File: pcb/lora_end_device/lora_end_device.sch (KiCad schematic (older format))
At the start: 27 parts, among them J1 USB_B_Micro, J2 UFL, J3 SMA, J4 UART, J5 Reset, J6 PRG, U1 TC1047A, U2 MCP6021, U3 LD1117, U4 RFM95W-868S2_mcc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

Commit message: fix bugs ERC
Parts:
- removed J1: USB_B_Micro, Connector_USB:USB_Micro-B_Molex-105133-0031, symbol Connector:USB_B_Micro
- added J1: USB_B_Micro, symbol Conector:USB_B_Micro
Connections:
- net GND: now also J1.5 (GND), J1.6 (Shield)
- net at D1.2 (A): now also J1.1 (VBUS)
- no-connect marks 0 -> 7
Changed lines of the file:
@@
-$EndComp
-$Comp
-L Diode:1N4007 D1
-U 1 1 60DF922B
-P 2550 6100
-F 0 "D1" H 2550 5883 50  0000 C CNN
-F 1 "1N4007" H 2550 5974 50  0000 C CNN
-F 2 "Diode_SMD:D_1206_3216Metric" H 2550 5925 50  0001 C CNN
-F 3 "http://www.vishay.com/docs/88503/1n4001.pdf" H 2550 6100 50  0001 C CNN
-	1    2550 6100
-	-1   0    0    1
 $EndComp
 $Comp
@@
 $EndComp
 $Comp
-L Connector:USB_B_Micro J1
-U 1 1 60DFF0A9
-P 1850 6300
-F 0 "J1" H 1907 6767 50  0000 C CNN
-F 1 "USB_B_Micro" H 1907 6676 50  0000 C CNN
-F 2 "Connector_USB:USB_Micro-B_Molex-105133-0031" H 2000 6250 50  0001 C CNN
-F 3 "~" H 2000 6250 50  0001 C CNN
-	1    1850 6300
-	1    0    0    -1
-$EndComp
-$Comp
-L power:GND #PWR03
-U 1 1 60EC034B
-P 1850 7000
-F 0 "#PWR03" H 1850 6750 50  0001 C CNN
-F 1 "GND" H 1855 6827 50  0000 C CNN
-F 2 "" H 1850 7000 50  0001 C CNN
-F 3 "" H 1850 7000 50  0001 C CNN
-	1    1850 7000
-	1    0    0    -1
-$EndComp
-$Comp
 L power:GND #PWR04
 U 1 1 60EC08DB
@@
 F 3 "" H 3350 6500 50  0001 C CNN
 	1    3350 6500
-	1    0    0    -1
-$EndComp
-$Comp
-L power:GND #PWR07
-U 1 1 60EC17F2
-P 4000 6500
-F 0 "#PWR07" H 4000 6250 50  0001 C CNN
-F 1 "GND" H 4005 6327 50  0000 C CNN
-F 2 "" H 4000 6500 50  0001 C CNN
-F 3 "" H 4000 6500 50  0001 C CNN
-	1    4000 6500
 	1    0    0    -1
 $EndComp
@@
 	2000 3450 2000 3250
 Wire Wire Line
-	2150 6100 2400 6100
-Wire Wire Line
-	2700 6100 2900 6100
-Wire Wire Line
 	2900 6100 3350 6100
 Connection ~ 2900 6100
 Wire Wire Line
-	3350 6100 3700 6100
-Connection ~ 3350 6100
-Wire Wire Line
 	4300 6100 4600 6100
-Wire Wire Line
-	1750 6700 1750 6750
-Wire Wire Line
-	1750 6750 1850 6750
-Wire Wire Line
-	1850 6750 1850 6700
-Wire Wire Line
-	1850 6750 1850 7000
-Connection ~ 1850 6750
 Wire Wire Line
 	4600 6100 4600 5700
 Connection ~ 4600 6100
-Wire Wire Line
-	4600 6400 4600 6500
 Wire Wire Line
 	4000 6400 4000 6500
@@
 	5600 1650 5600 2100
 Wire Notes Line
-	5250 5250 5250 7350
-Wire Notes Line
 	1300 5250 5250 5250
 Wire Wire Line
-	9950 3900 9950 4000
-Wire Wire Line
-	10050 3900 9950 3900
-Wire Wire Line
 	9950 4600 9950 4700
 Wire Wire Line
 	10050 4600 9950 4600
 $Comp
-L power:GND #PWR?
+L power:GND #PWR0101
 U 1 1 61107347
 P 9950 4700
-F 0 "#PWR?" H 9950 4450 50  0001 C CNN
+F 0 "#PWR0101" H 9950 4450 50  0001 C CNN
 F 1 "GND" H 9955 4527 50  0000 C CNN
 F 2 "" H 9950 4700 50  0001 C CNN
@@
 $EndComp
 $Comp
-L power:GND #PWR?
+L power:GND #PWR0102
 U 1 1 61106BAC
-P 9950 4000
-F 0 "#PWR?" H 9950 3750 50  0001 C CNN
-F 1 "GND" H 9955 3827 50  0000 C CNN
-F 2 "" H 9950 4000 50  0001 C CNN
-F 3 "" H 9950 4000 50  0001 C CNN
-	1    9950 4000
+P 9950 4100
+F 0 "#PWR0102" H 9950 3850 50  0001 C CNN
+F 1 "GND" H 9955 3927 50  0000 C CNN
+F 2 "" H 9950 4100 50  0001 C CNN
+F 3 "" H 9950 4100 50  0001 C CNN
+	1    9950 4100
 	1    0    0    -1
 $EndComp
@@
 Conectores de antena
 $Comp
-L power:GND #PWR?
+L power:GND #PWR0103
 U 1 1 611C175D
 P 3650 4200
-F 0 "#PWR?" H 3650 3950 50  0001 C CNN
+F 0 "#PWR0103" H 3650 3950 50  0001 C CNN
 F 1 "GND" H 3655 4027 50  0000 C CNN
 F 2 "" H 3650 4200 50  0001 C CNN
@@
 $EndComp
 $Comp
-L power:+3.3V #PWR?
+L power:+3.3V #PWR0104
 U 1 1 611C2640
 P 3650 3050
-F 0 "#PWR?" H 3650 2900 50  0001 C CNN
+F 0 "#PWR0104" H 3650 2900 50  0001 C CNN
 F 1 "+3.3V" H 3665 3223 50  0000 C CNN
 F 2 "" H 3650 3050 50  0001 C CNN
@@
 Wire Wire Line
 	6000 4400 7750 4400
+NoConn ~ 6350 3350
+NoConn ~ 6350 3450
+NoConn ~ 6350 3550
+NoConn ~ 6350 3650
+NoConn ~ 2150 6300
+NoConn ~ 2150 6400
+NoConn ~ 2150 6500
+Wire Wire Line
+	3350 6100 3550 6100
+Connection ~ 3350 6100
+Wire Wire Line
+	1850 6700 1850 6800
+$Comp
+L Conector:USB_B_Micro J1
+U 1 1 6125ECC1
+P 1850 6300
+F 0 "J1" H 1907 6767 50  0000 C CNN
+F 1 "USB_B_Micro" H 1907 6676 50  0000 C CNN
+F 2 "" H 2000 6250 50  0001 C CNN
+F 3 "~" H 2000 6250 50  0001 C CNN
+	1    1850 6300
+	1    0    0    -1
+$EndComp
+Wire Wire Line
+	1750 6700 1750 6800
+Wire Wire Line
+	1750 6800 1850 6800
+Wire Wire Line
+	2700 6100 2900 6100
+Wire Wire Line
+	2150 6100 2400 6100
+$Comp
+L Diode:1N4007 D1
+U 1 1 60DF922B
+P 2550 6100
+F 0 "D1" H 2550 5883 50  0000 C CNN
+F 1 "1N4007" H 2550 5974 50  0000 C CNN
+F 2 "Diode_SMD:D_1206_3216Metric" H 2550 5925 50  0001 C CNN
+F 3 "http://www.vishay.com/docs/88503/1n4001.pdf" H 2550 6100 50  0001 C CNN
+	1    2550 6100
+	-1   0    0    1
+$EndComp
+Connection ~ 1850 6800
+$Comp
+L power:GND #PWR03
+U 1 1 60EC034B
+P 1850 7100
+F 0 "#PWR03" H 1850 6850 50  0001 C CNN
+F 1 "GND" H 1855 6927 50  0000 C CNN
+F 2 "" H 1850 7100 50  0001 C CNN
+F 3 "" H 1850 7100 50  0001 C CNN
+	1    1850 7100
+	1    0    0    -1
+$EndComp
+Wire Wire Line
+	1850 6800 1850 7100
+Wire Wire Line
+	10050 3900 9950 3900
+Wire Wire Line
+	9950 3900 9950 4100
+Wire Wire Line
+	3550 5950 3550 6100
+Connection ~ 3550 6100
+Wire Wire Line
+	3550 6100 3700 6100
+$Comp
+L power:PWR_FLAG #FLG0101
+U 1 1 612BB4E2
+P 3550 5950
+F 0 "#FLG0101" H 3550 6025 50  0001 C CNN
+F 1 "PWR_FLAG" H 3550 6123 50  0000 C CNN
+F 2 "" H 3550 5950 50  0001 C CNN
+F 3 "~" H 3550 5950 50  0001 C CNN
+	1    3550 5950
+	1    0    0    -1
+$EndComp
+Wire Notes Line
+	5250 5250 5250 7350
+Wire Wire Line
+	4600 6400 4600 6500
+$Comp
+L power:GND #PWR07
+U 1 1 60EC17F2
+P 4000 6500
+F 0 "#PWR07" H 4000 6250 50  0001 C CNN
+F 1 "GND" H 4005 6327 50  0000 C CNN
+F 2 "" H 4000 6500 50  0001 C CNN
+F 3 "" H 4000 6500 50  0001 C CNN
+	1    4000 6500
+	1    0    0    -1
+$EndComp
+$Comp
+L power:PWR_FLAG #FLG0102
+U 1 1 60E3DDB4
+P 5000 6850
+F 0 "#FLG0102" H 5000 6925 50  0001 C CNN
+F 1 "PWR_FLAG" H 5000 7023 50  0000 C CNN
+F 2 "" H 5000 6850 50  0001 C CNN
+F 3 "~" H 5000 6850 50  0001 C CNN
+	1    5000 6850
+	1    0    0    -1
+$EndComp
+$Comp
+L power:GND #PWR0105
+U 1 1 60E3E607
+P 5000 7050
+F 0 "#PWR0105" H 5000 6800 50  0001 C CNN
+F 1 "GND" H 5005 6877 50  0000 C CNN
+F 2 "" H 5000 7050 50  0001 C CNN
+F 3 "" H 5000 7050 50  0001 C CNN
+	1    5000 7050
+	1    0    0    -1
+$EndComp
+Wire Wire Line
+	5000 6850 5000 7050
 $EndSCHEMATC

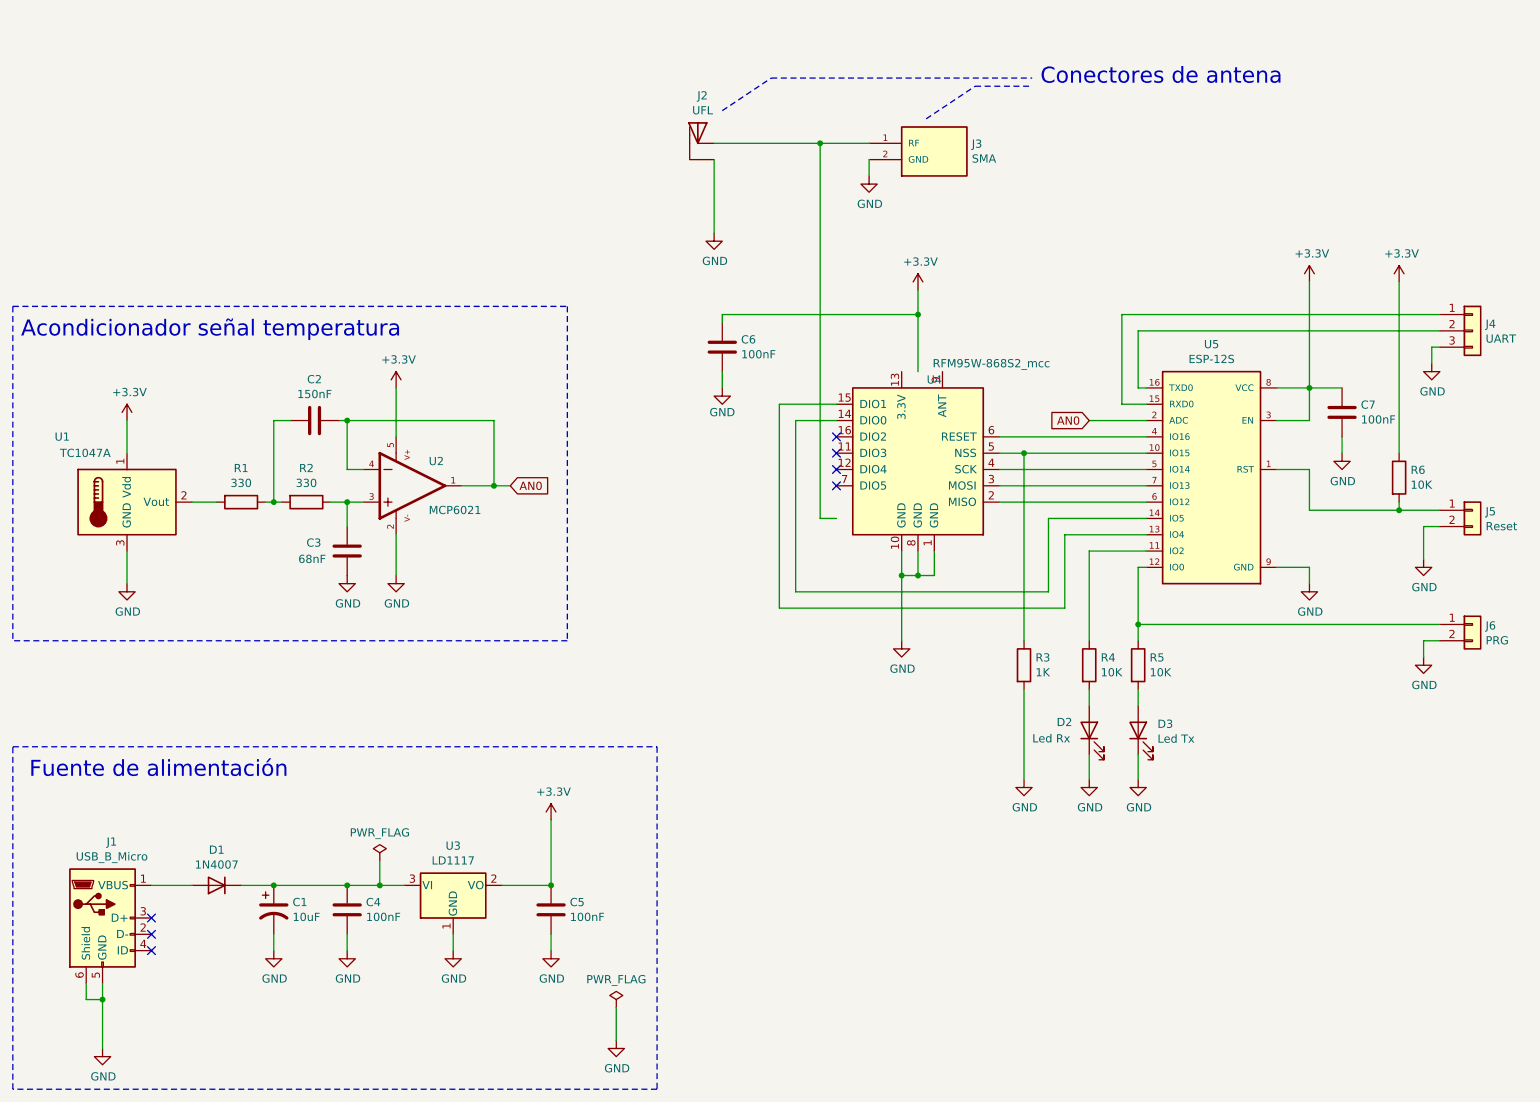
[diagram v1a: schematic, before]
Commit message: add asociaciones footprint, orificios fijacion
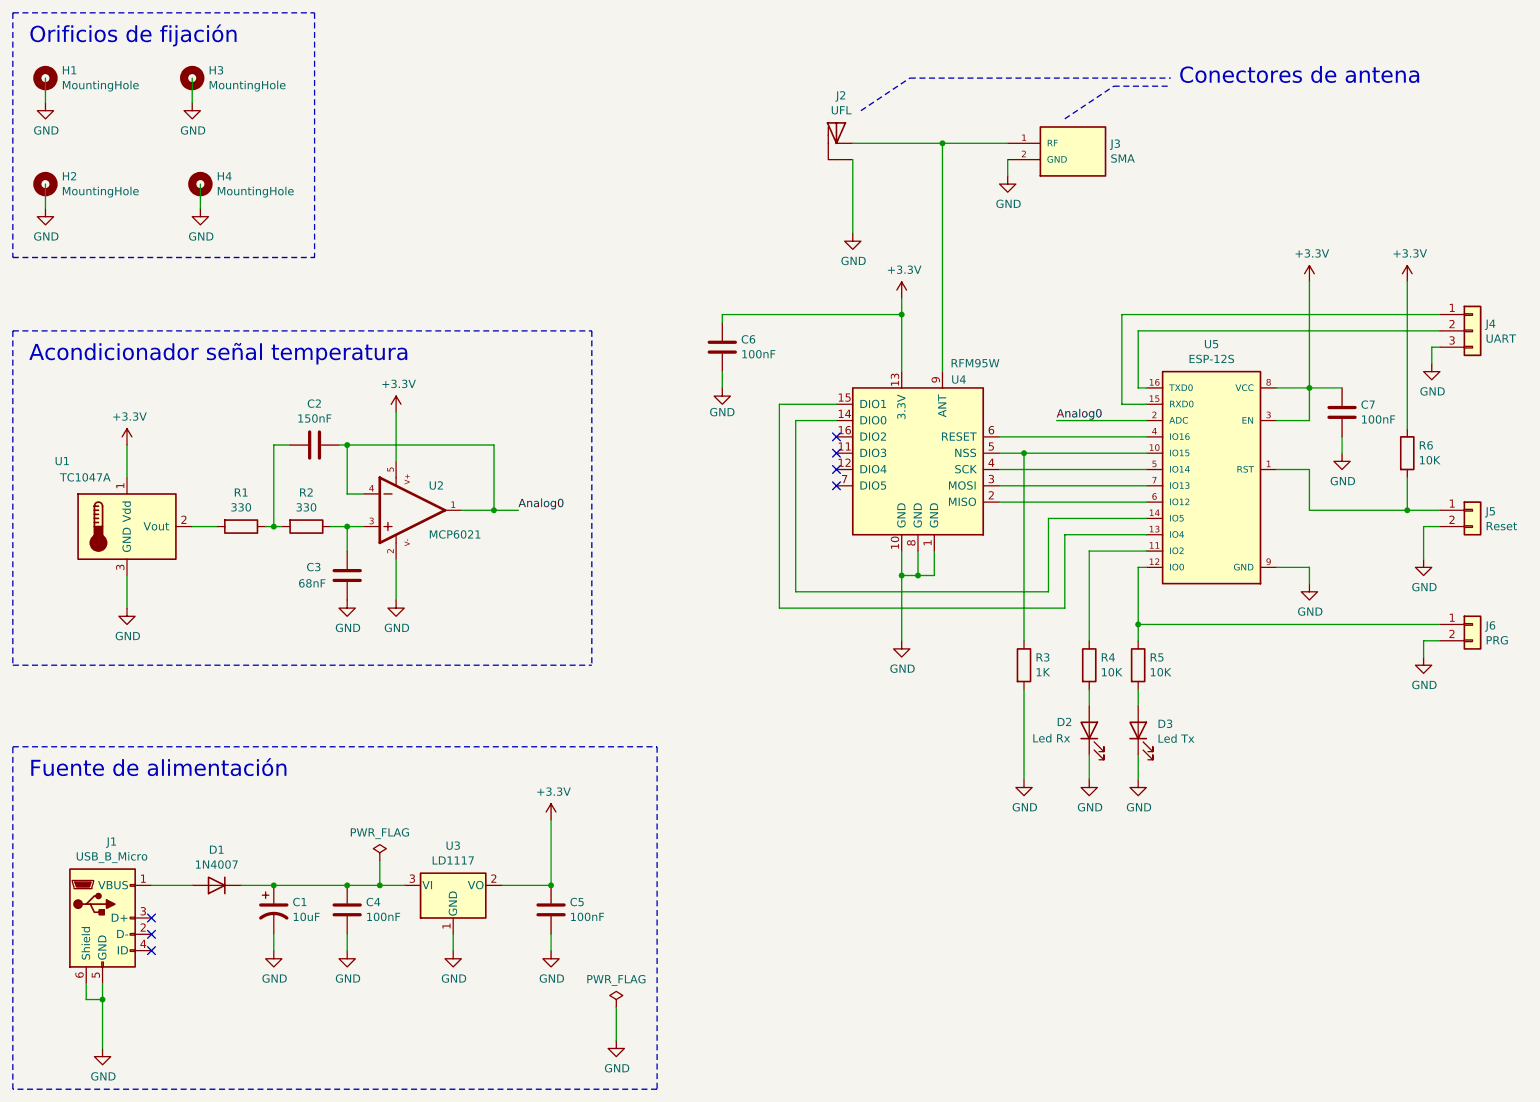
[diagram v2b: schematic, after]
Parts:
- added H1, H2, H3, H4: MountingHole, MountingHole:MountingHole_3.2mm_M3, symbol Mechanical:MountingHole
- C1: footprint (none) -> Capacitor_SMD:CP_Elec_3x5.3
- J1: footprint (none) -> Connector_USB:USB_Mini-B_Lumberg_2486_01_Horizontal
- J4: footprint Connector_PinHeader_2.00mm:PinHeader_1x03_P2.00mm_Vertical -> Connector_PinHeader_2.54mm:PinHeader_1x03_P2.54mm_Vertical
- J5, J6: footprint Connector_PinHeader_2.00mm:PinHeader_1x02_P2.00mm_Vertical -> Connector_PinHeader_2.54mm:PinHeader_1x02_P2.54mm_Vertical
- U4: value RFM95W-868S2_mcc -> RFM95W
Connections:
- net labels added: Analog0
- net labels removed: AN0
- wire segments 108 -> 111
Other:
- note added: "Orificios de fijación"
- moved on the sheet: C2, C3, J2, J3, R1, R2, R6, U1, U2
